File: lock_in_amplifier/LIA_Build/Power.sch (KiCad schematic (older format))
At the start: 58 parts, among them J1 vref-in, J19 +3V3 OUT, J2 vref, J3 V-IN, J4 GND, J46 -5V OUT, J47 +5V OUT, J5 V+IN, J6 +5V, J7 +3V3, J8 -5V, Q1 DMN640L, Q2 DMN640L, U1 LM358, U2 lm7805, U3 LM7833, U4 lm7905

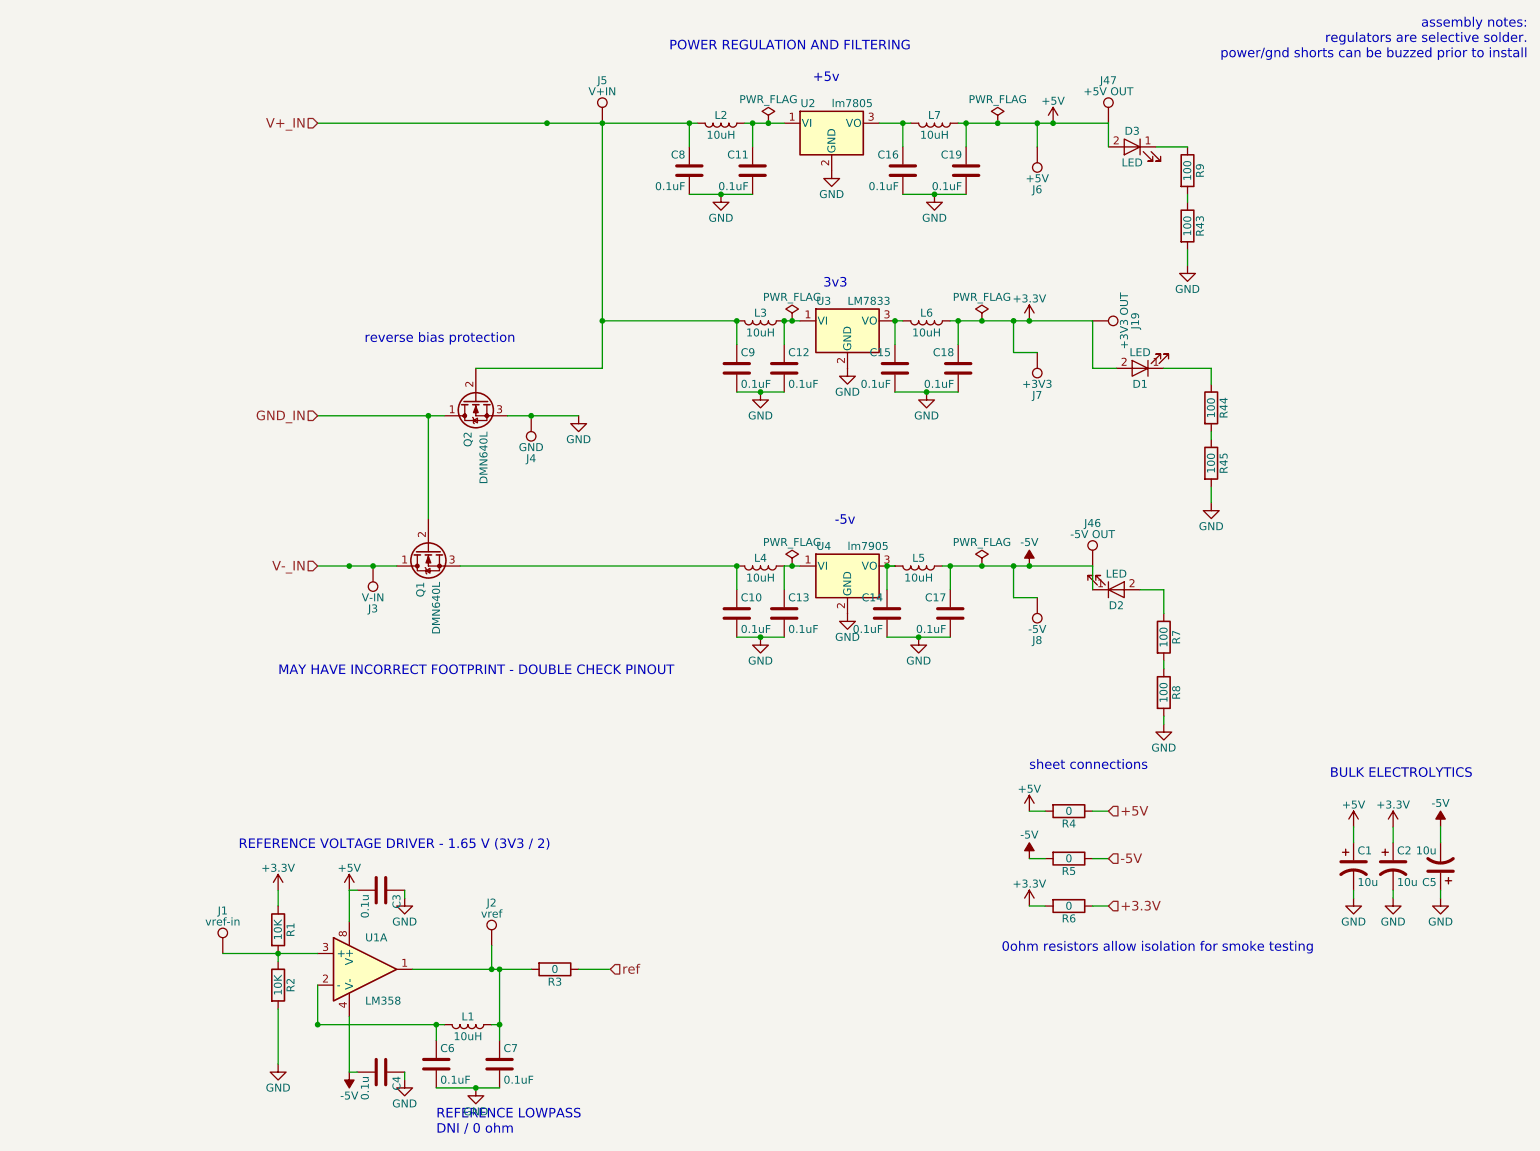
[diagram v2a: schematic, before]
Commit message: switch footprints, lm833 usage, pll investigation
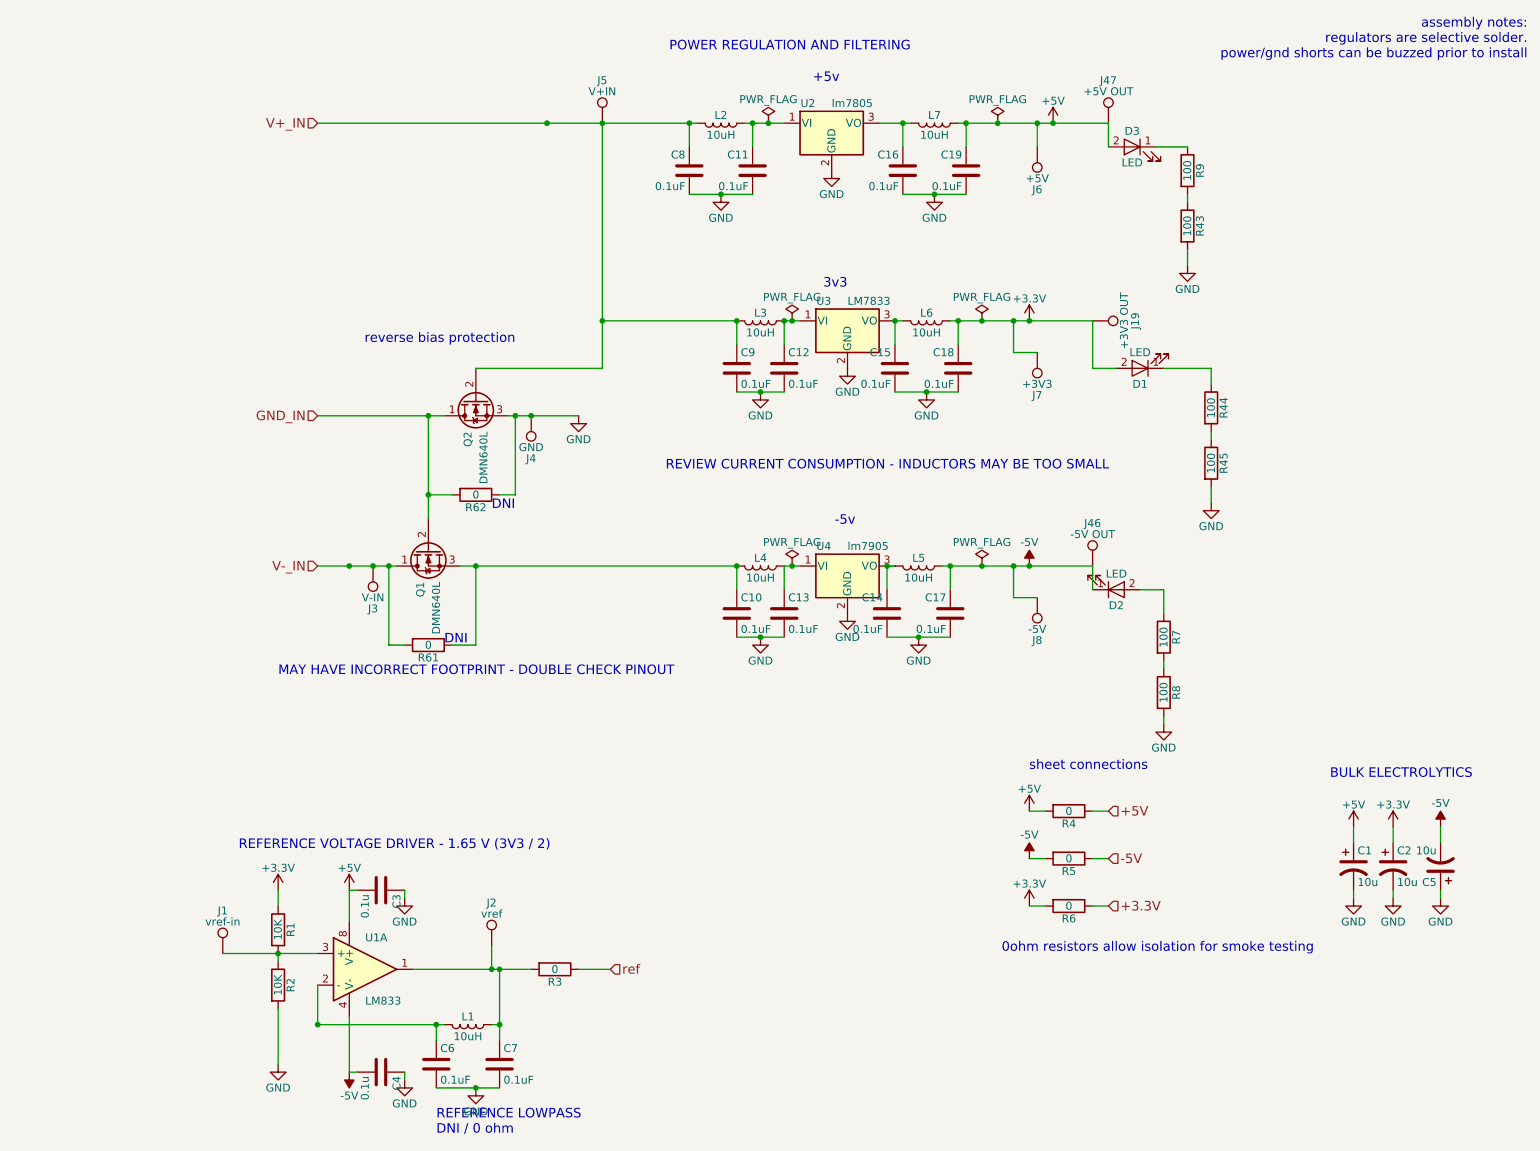
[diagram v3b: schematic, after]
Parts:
- added R61, R62: 0, symbol R
- U1: value LM358 -> LM833
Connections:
- net GND: now also R62.1
- net GND_IN: now also R62.2
- net V-_IN: now also R61.2
- net at C10.1, L4.2, Q1.3 (S): now also R61.1
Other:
- note added: "DNI"
- note added: "REVIEW CURRENT CONSUMPTION - INDUCTORS MAY BE TOO SMALL"
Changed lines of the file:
@@
 P 2950 6700
 F 0 "U1" H 2950 6900 50  0000 L CNN
-F 1 "LM358" H 2950 6500 50  0000 L CNN
+F 1 "LM833" H 2950 6500 50  0000 L CNN
 F 2 "SMD_Packages:SOIC-8-N" H 2950 6700 50  0001 C CNN
 F 3 "" H 2950 6700 50  0001 C CNN
@@
 Wire Wire Line
 	8000 5150 8000 5100
+Text Notes 4850 3550 0    60   ~ 0
+REVIEW CURRENT CONSUMPTION - INDUCTORS MAY BE TOO SMALL
+$Comp
+L R R62
+U 1 1 5A23FE01
+P 3650 3700
+F 0 "R62" V 3730 3700 50  0000 C CNN
+F 1 "0" V 3650 3700 50  0000 C CNN
+F 2 "" V 3580 3700 50  0001 C CNN
+F 3 "" H 3650 3700 50  0001 C CNN
+	1    3650 3700
+	0    1    1    0
+$EndComp
+$Comp
+L R R61
+U 1 1 5A23FF66
+P 3350 4650
+F 0 "R61" V 3430 4650 50  0000 C CNN
+F 1 "0" V 3350 4650 50  0000 C CNN
+F 2 "" V 3280 4650 50  0001 C CNN
+F 3 "" H 3350 4650 50  0001 C CNN
+	1    3350 4650
+	0    1    1    0
+$EndComp
+Wire Wire Line
+	3500 4650 3650 4650
+Wire Wire Line
+	3650 4650 3650 4150
+Connection ~ 3650 4150
+Wire Wire Line
+	3200 4650 3100 4650
+Wire Wire Line
+	3100 4650 3100 4150
+Connection ~ 3100 4150
+Text Notes 3450 4650 0    60   ~ 0
+DNI
+Wire Wire Line
+	3800 3700 3900 3700
+Wire Wire Line
+	3900 3700 3900 3200
+Connection ~ 3900 3200
+Wire Wire Line
+	3500 3700 3350 3700
+Connection ~ 3350 3700
+Text Notes 3750 3800 0    60   ~ 0
+DNI
 $EndSCHEMATC

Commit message: pll finalized - misc cleanup - review candidate
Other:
- note added: "0 OHM FOR POWER SUPPLY CHECKOUT"
- note added: "REVERSE BIAS PROTECTION"
- note removed: "0ohm resistors allow isolation for smoke testing"
- note removed: "MAY HAVE INCORRECT FOOTPRINT - DOUBLE CHECK PINOUT"
- note removed: "REVIEW CURRENT CONSUMPTION - INDUCTORS MAY BE TOO SMALL"
- note removed: "assembly notes:\nregulators are selective solder.\npower/gnd shorts can be buzzed prior to install\n"
- note removed: "reverse bias protection"
